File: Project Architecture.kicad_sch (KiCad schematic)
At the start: 0 parts

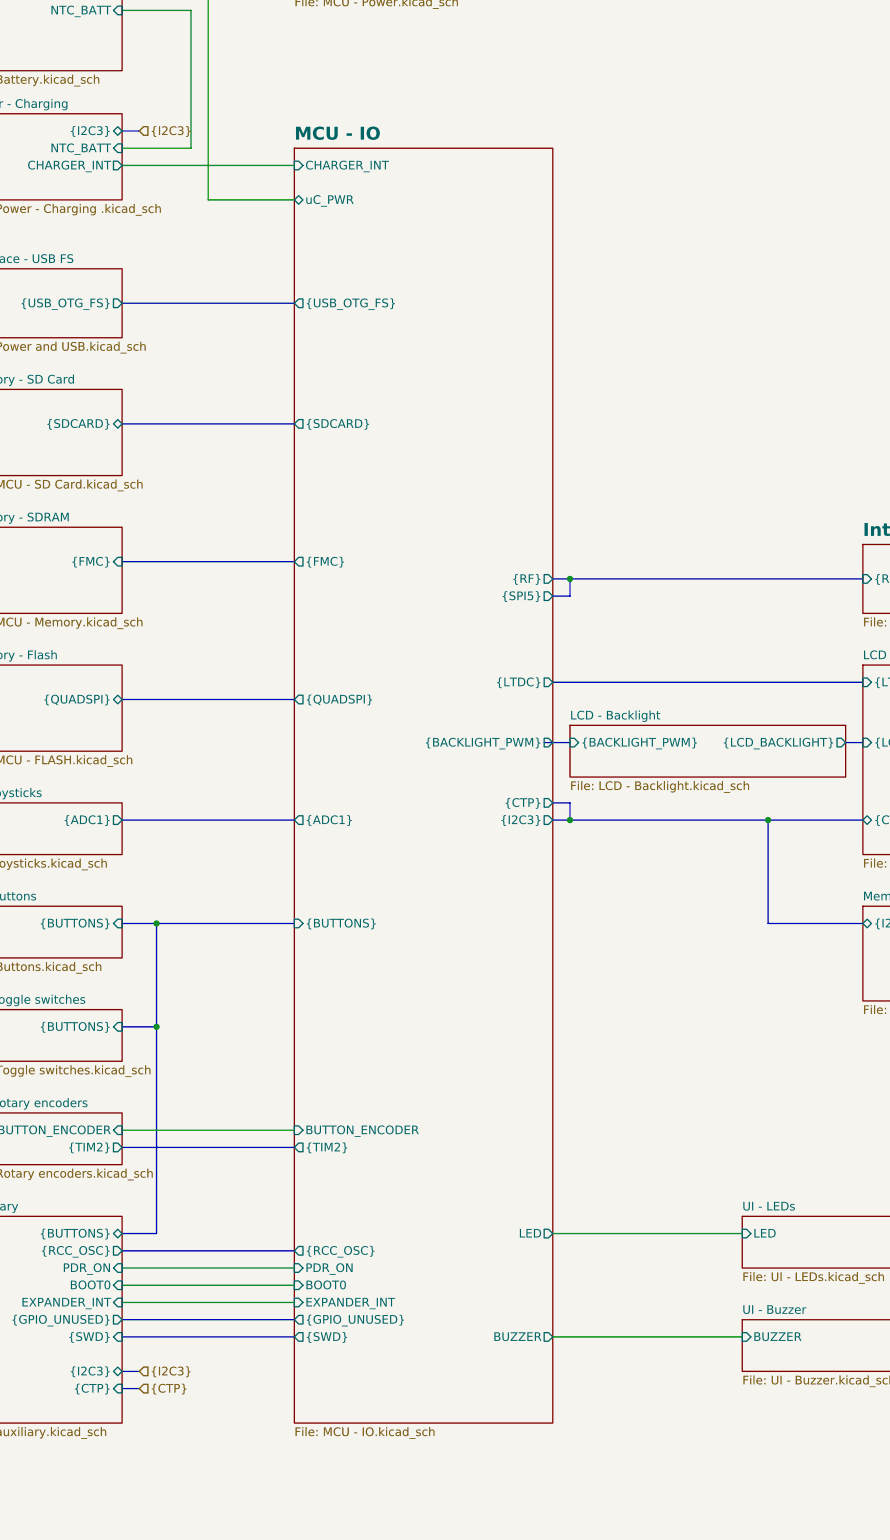
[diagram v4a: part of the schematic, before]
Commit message: duzo zmian, layout przetwornic i zasilania, wstepny routing sd card impedance control, usb differential impedance control
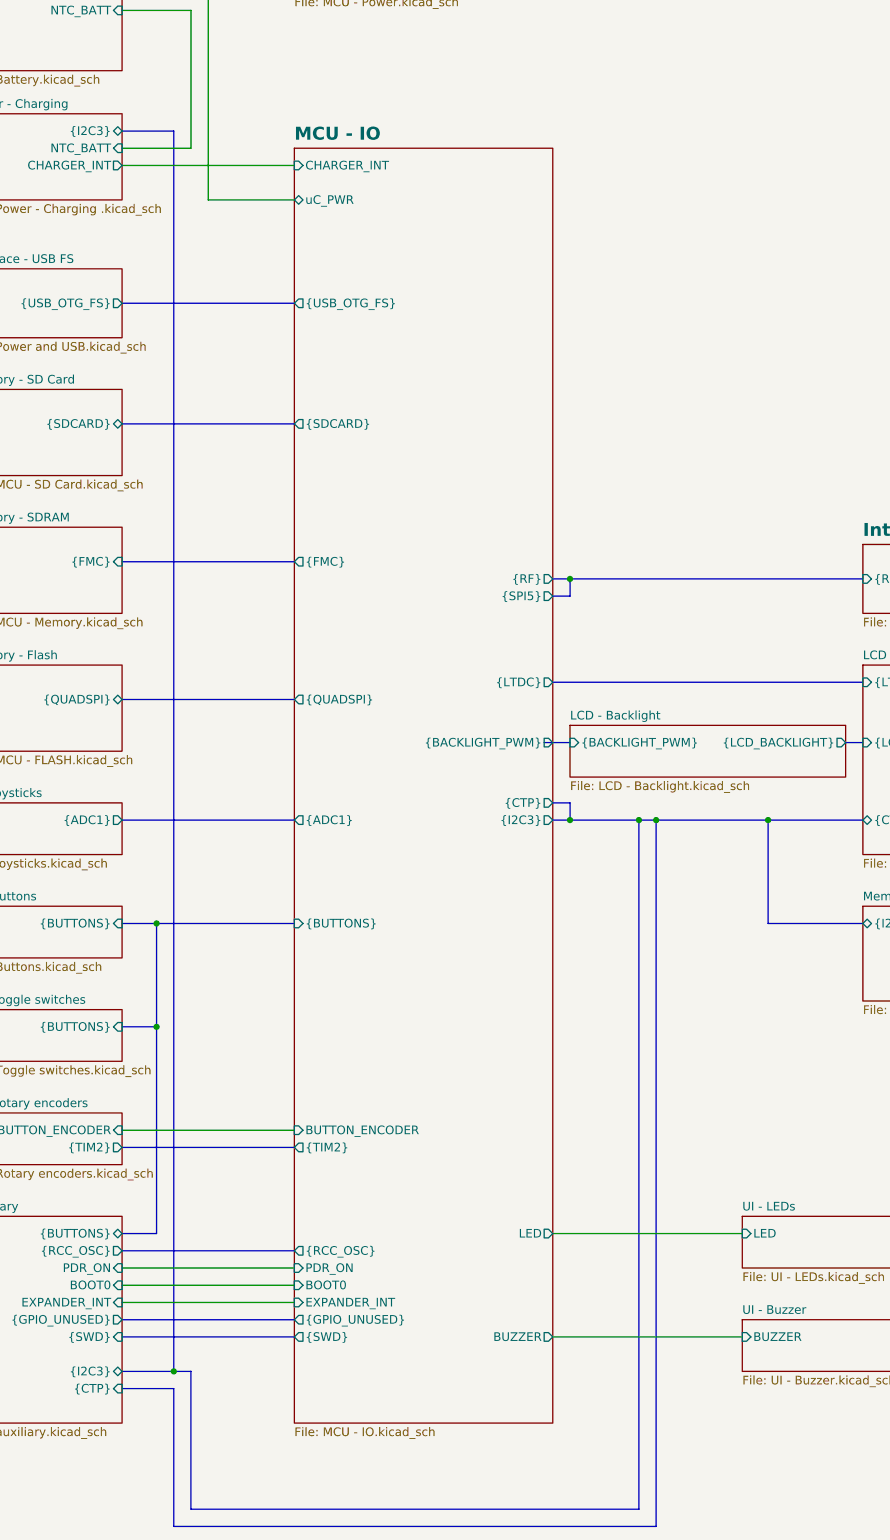
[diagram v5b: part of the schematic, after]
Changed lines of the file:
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@@
+	)
+	(junction
+		(at 119.38 307.34)
+		(diameter 0)
+		(color 0 0 0 0)
 	)
 	(junction
@@
 	)
 	(junction
+		(at 187.96 226.06)
+		(diameter 0)
+		(color 0 0 0 0)
+	)
+	(junction
 		(at 177.8 226.06)
 		(diameter 0)
@@
 		(color 0 0 0 0)
 	)
+	(junction
+		(at 190.5 226.06)
+		(diameter 0)
+		(color 0 0 0 0)
+	)
 	(wire
 		(pts
@@
 	(bus
 		(pts
-			(xy 111.76 124.46) (xy 114.3 124.46)
+			(xy 121.92 327.66) (xy 187.96 327.66)
+		)
+		(stroke
+			(width 0)
+			(type default)
+		)
+	)
+	(bus
+		(pts
+			(xy 119.38 330.2) (xy 190.5 330.2)
+		)
+		(stroke
+			(width 0)
+			(type default)
+		)
+	)
+	(bus
+		(pts
+			(xy 111.76 124.46) (xy 119.38 124.46)
 		)
 		(stroke
@@
 	(bus
 		(pts
+			(xy 190.5 226.06) (xy 190.5 330.2)
+		)
+		(stroke
+			(width 0)
+			(type default)
+		)
+	)
+	(bus
+		(pts
 			(xy 207.01 241.3) (xy 220.98 241.3)
 		)
@@
 	(bus
 		(pts
-			(xy 177.8 226.06) (xy 207.01 226.06)
+			(xy 177.8 226.06) (xy 187.96 226.06)
+		)
+		(stroke
+			(width 0)
+			(type default)
+		)
+	)
+	(bus
+		(pts
+			(xy 187.96 226.06) (xy 187.96 327.66)
+		)
+		(stroke
+			(width 0)
+			(type default)
+		)
+	)
+	(bus
+		(pts
+			(xy 119.38 309.88) (xy 119.38 330.2)
 		)
 		(stroke
@@
 	(bus
 		(pts
-			(xy 111.76 309.88) (xy 114.3 309.88)
+			(xy 111.76 309.88) (xy 119.38 309.88)
 		)
 		(stroke
@@
 	(bus
 		(pts
+			(xy 121.92 307.34) (xy 121.92 327.66)
+		)
+		(stroke
+			(width 0)
+			(type default)
+		)
+	)
+	(bus
+		(pts
 			(xy 116.84 241.3) (xy 116.84 256.54)
 		)
@@
 		)
 	)
+	(bus
+		(pts
+			(xy 119.38 124.46) (xy 119.38 307.34)
+		)
+		(stroke
+			(width 0)
+			(type default)
+		)
+	)
 	(wire
 		(pts
@@
 	(bus
 		(pts
+			(xy 190.5 226.06) (xy 207.01 226.06)
+		)
+		(stroke
+			(width 0)
+			(type default)
+		)
+	)
+	(bus
+		(pts
 			(xy 111.76 289.56) (xy 137.16 289.56)
 		)
@@
 	(bus
 		(pts
+			(xy 119.38 307.34) (xy 121.92 307.34)
+		)
+		(stroke
+			(width 0)
+			(type default)
+		)
+	)
+	(bus
+		(pts
 			(xy 111.76 226.06) (xy 137.16 226.06)
 		)
@@
 	(bus
 		(pts
+			(xy 187.96 226.06) (xy 190.5 226.06)
+		)
+		(stroke
+			(width 0)
+			(type default)
+		)
+	)
+	(bus
+		(pts
 			(xy 175.26 226.06) (xy 177.8 226.06)
 		)
@@
 	(bus
 		(pts
-			(xy 111.76 307.34) (xy 114.3 307.34)
-		)
-		(stroke
-			(width 0)
-			(type default)
-		)
-	)
-	(hierarchical_label "{I2C3}"
-		(shape input)
-		(at 114.3 307.34 0)
-		(effects
-			(font
-				(size 1.27 1.27)
-			)
-			(justify left)
-		)
-	)
-	(hierarchical_label "{CTP}"
-		(shape input)
-		(at 114.3 309.88 0)
-		(effects
-			(font
-				(size 1.27 1.27)
-			)
-			(justify left)
-		)
-	)
-	(hierarchical_label "{I2C3}"
-		(shape input)
-		(at 114.3 124.46 0)
-		(effects
-			(font
-				(size 1.27 1.27)
-			)
-			(justify left)
-		)
-	)
+			(xy 111.76 307.34) (xy 119.38 307.34)
+		)
+		(stroke
+			(width 0)
+			(type default)
+		)
+	)

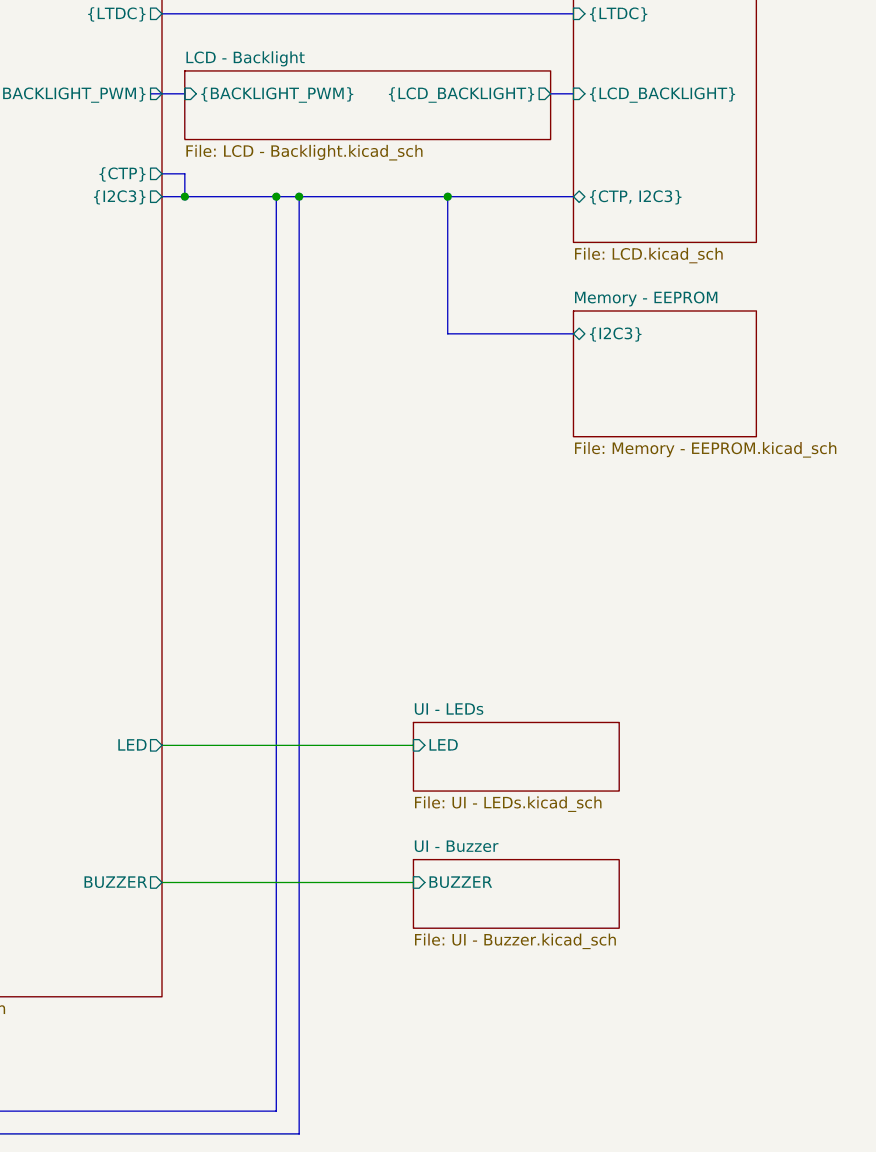
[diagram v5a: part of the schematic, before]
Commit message: qspi layout, length matching, sdcard lengthmatching, change some footprints, prototype production generation
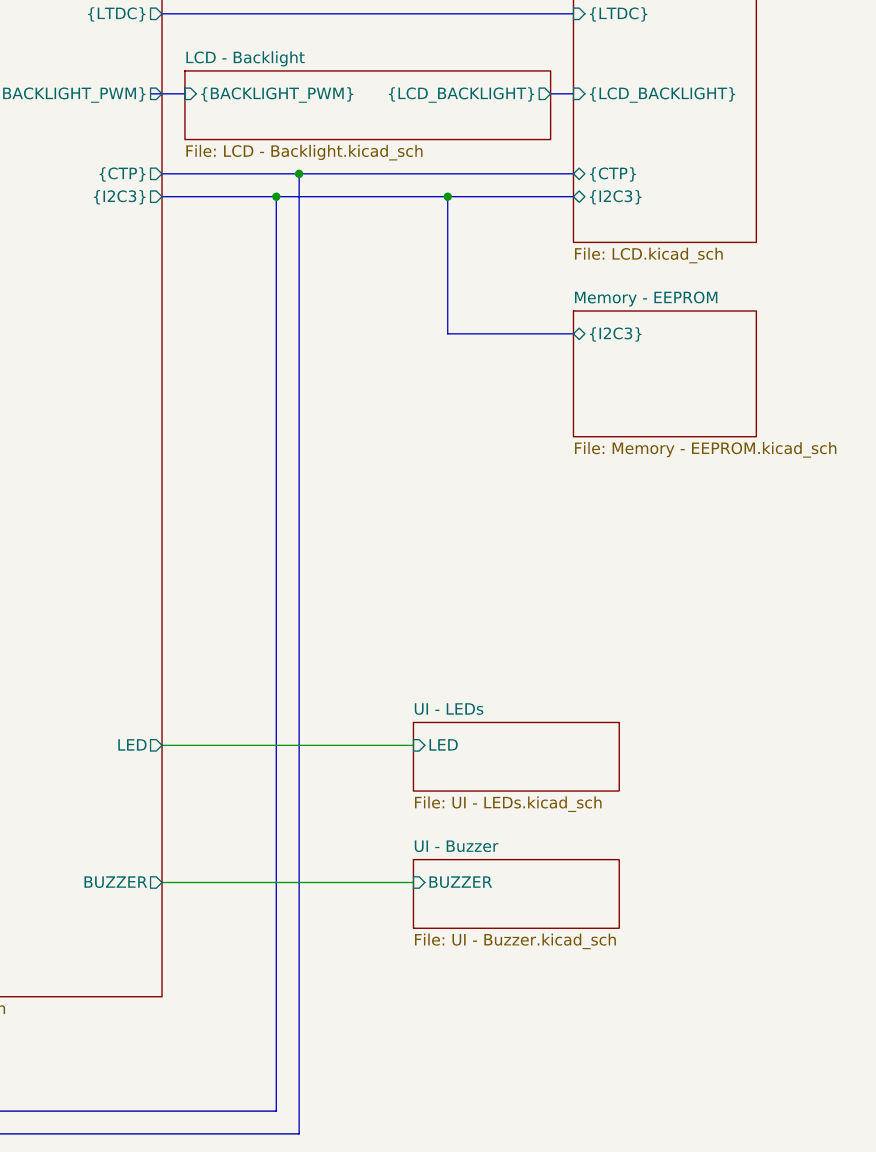
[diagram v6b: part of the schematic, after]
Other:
- sheet LCD - Connectors ports: added {CTP}, {I2C3}; removed {CTP, I2C3}
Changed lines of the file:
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@@
+	)
+	(junction
+		(at 190.5 223.52)
+		(diameter 0)
+		(color 0 0 0 0)
 	)
 	(junction
@@
 	)
 	(junction
-		(at 177.8 226.06)
-		(diameter 0)
-		(color 0 0 0 0)
-	)
-	(junction
 		(at 116.84 241.3)
 		(diameter 0)
 		(color 0 0 0 0)
 	)
-	(junction
-		(at 190.5 226.06)
-		(diameter 0)
-		(color 0 0 0 0)
+	(bus
+		(pts
+			(xy 190.5 223.52) (xy 220.98 223.52)
+		)
+		(stroke
+			(width 0)
+			(type default)
+		)
 	)
 	(wire
@@
 	(bus
 		(pts
-			(xy 177.8 223.52) (xy 177.8 226.06)
+			(xy 190.5 223.52) (xy 190.5 330.2)
 		)
 		(stroke
@@
 	(bus
 		(pts
-			(xy 190.5 226.06) (xy 190.5 330.2)
-		)
-		(stroke
-			(width 0)
-			(type default)
-		)
-	)
-	(bus
-		(pts
 			(xy 207.01 241.3) (xy 220.98 241.3)
 		)
@@
 	(bus
 		(pts
-			(xy 177.8 226.06) (xy 187.96 226.06)
+			(xy 175.26 226.06) (xy 187.96 226.06)
 		)
 		(stroke
@@
 	(bus
 		(pts
-			(xy 190.5 226.06) (xy 207.01 226.06)
+			(xy 187.96 226.06) (xy 207.01 226.06)
 		)
 		(stroke
@@
 	(bus
 		(pts
-			(xy 175.26 223.52) (xy 177.8 223.52)
+			(xy 175.26 223.52) (xy 190.5 223.52)
 		)
 		(stroke
@@
 		(pts
 			(xy 111.76 294.64) (xy 137.16 294.64)
-		)
-		(stroke
-			(width 0)
-			(type default)
-		)
-	)
-	(bus
-		(pts
-			(xy 187.96 226.06) (xy 190.5 226.06)
-		)
-		(stroke
-			(width 0)
-			(type default)
-		)
-	)
-	(bus
-		(pts
-			(xy 175.26 226.06) (xy 177.8 226.06)
 		)
 		(stroke
@@
 			)
 		)
-		(pin "{CTP, I2C3}" bidirectional
-			(at 220.98 226.06 180)
-			(effects
-				(font
-					(size 1.27 1.27)
-				)
-				(justify left)
-			)
-		)
 		(pin "{LCD_BACKLIGHT}" input
 			(at 220.98 214.63 180)
 			(effects
 				(font
+					(size 1.27 1.27)
+				)
+				(justify left)
+			)
+		)
+		(pin "{CTP}" bidirectional
+			(at 220.98 223.52 180)
+			(effects
+				(font
+					(size 1.27 1.27)
+				)
+				(justify left)
+			)
+		)
+		(pin "{I2C3}" bidirectional
+			(at 220.98 226.06 180)
+			(effects
+				(font

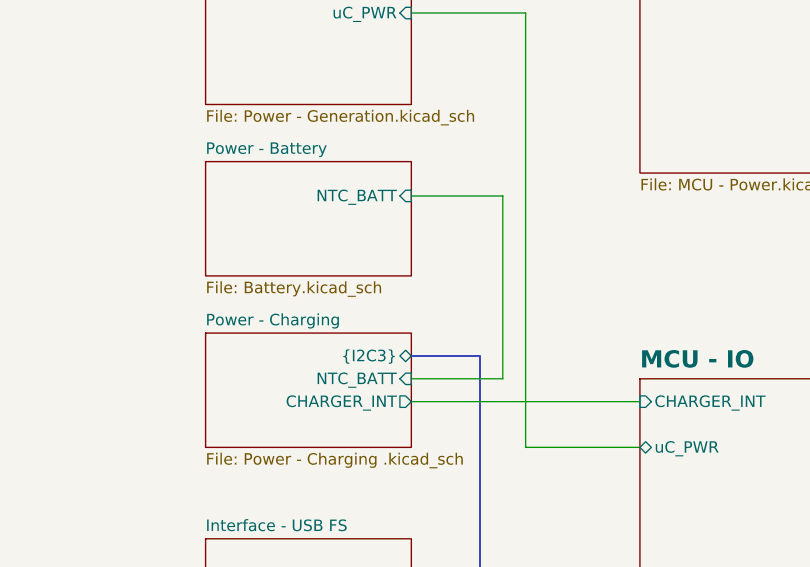
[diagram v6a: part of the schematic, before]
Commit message: added gas guage IC for monitoring battery
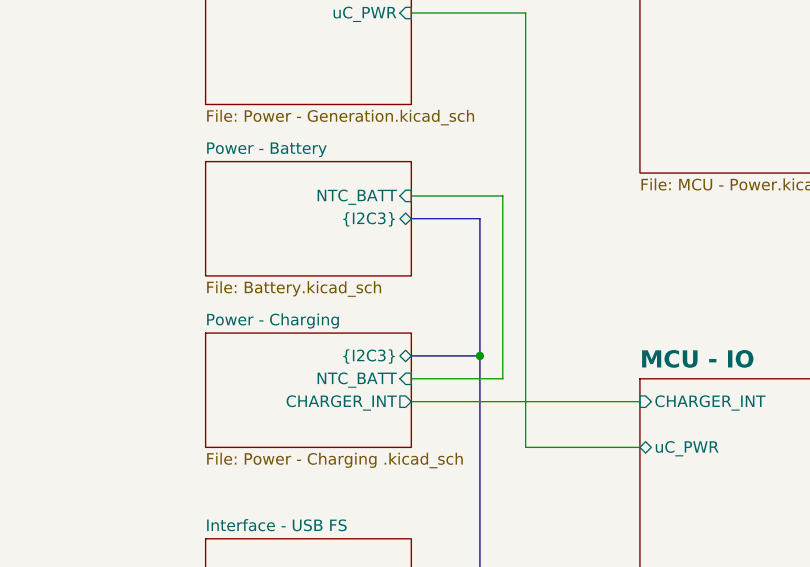
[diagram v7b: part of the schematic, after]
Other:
- sheet Power - Battery ports: added {I2C3}; removed none
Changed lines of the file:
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@@
 		(color 0 0 0 0)
 	)
+	(junction
+		(at 119.38 124.46)
+		(diameter 0)
+		(color 0 0 0 0)
+	)
 	(bus
 		(pts
@@
 		)
 	)
+	(bus
+		(pts
+			(xy 111.76 109.22) (xy 119.38 109.22)
+		)
+		(stroke
+			(width 0)
+			(type default)
+		)
+	)
 	(wire
 		(pts
@@
 			(width 0)
 			(type dash)
+		)
+	)
+	(bus
+		(pts
+			(xy 119.38 109.22) (xy 119.38 124.46)
+		)
+		(stroke
+			(width 0)
+			(type default)
 		)
 	)
@@
 			(effects
 				(font
+					(size 1.27 1.27)
+				)
+				(justify right)
+			)
+		)
+		(pin "{I2C3}" bidirectional
+			(at 111.76 109.22 0)
+			(effects
+				(font
